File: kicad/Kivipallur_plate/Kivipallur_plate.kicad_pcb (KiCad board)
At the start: 2 copper layers, 158.1 x 105.3 mm, 12 parts

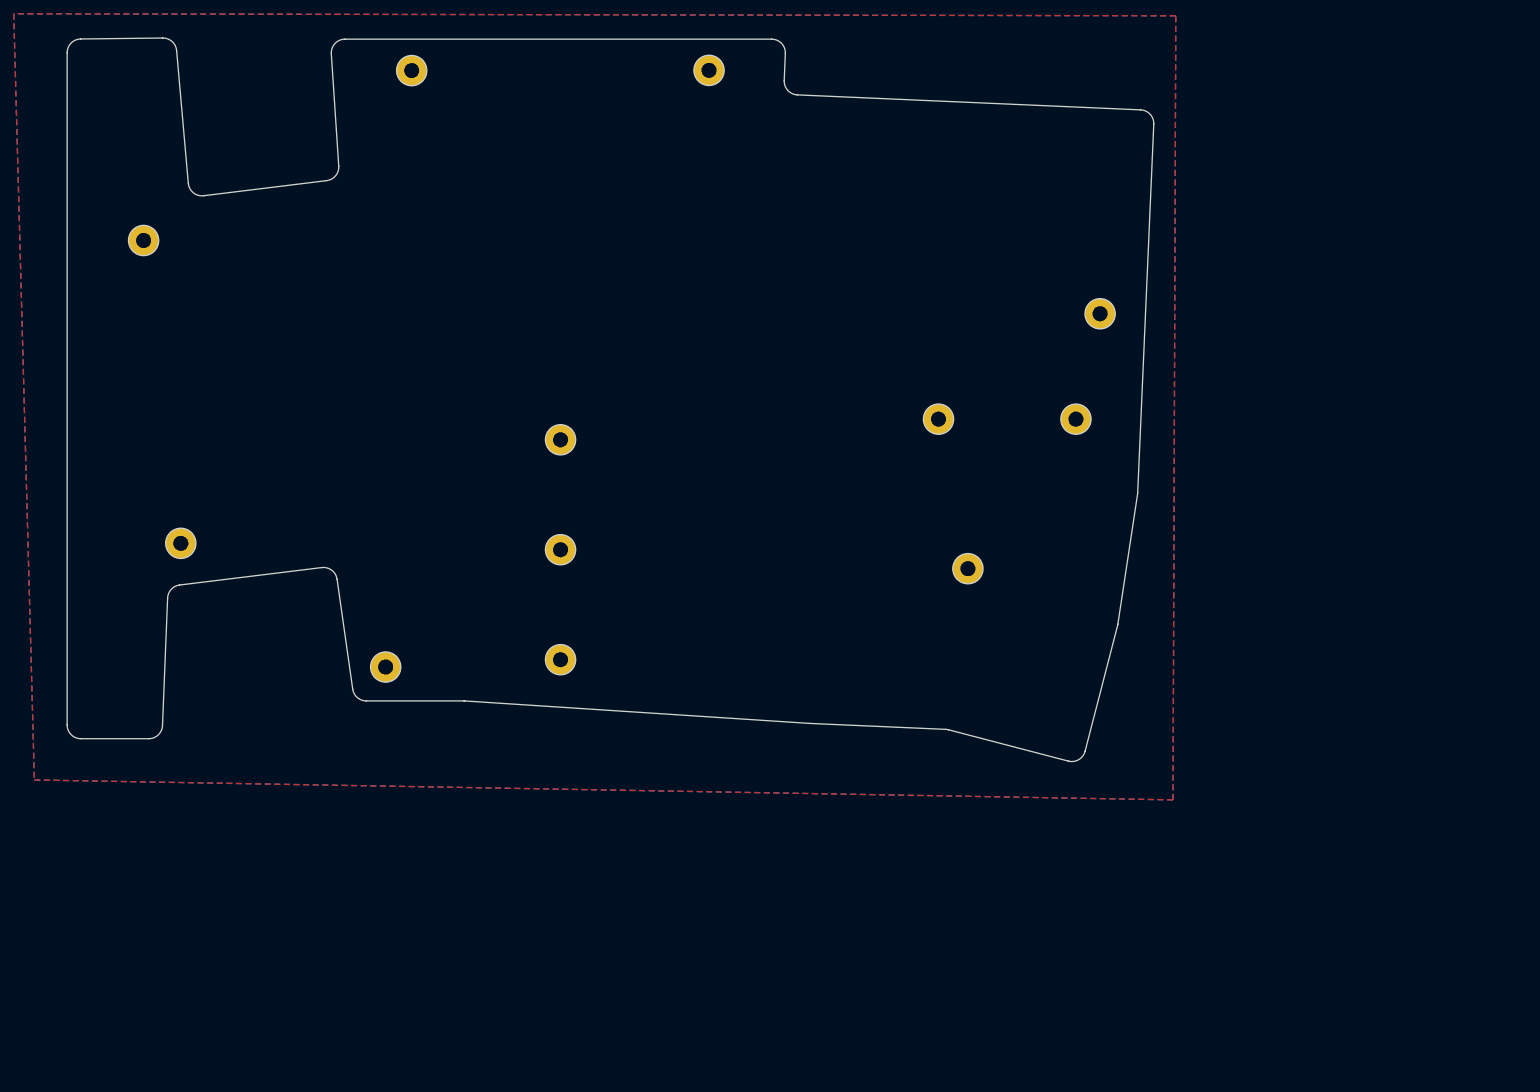
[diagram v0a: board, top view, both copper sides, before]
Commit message: Change PMW3360 footprint outline, finalize others
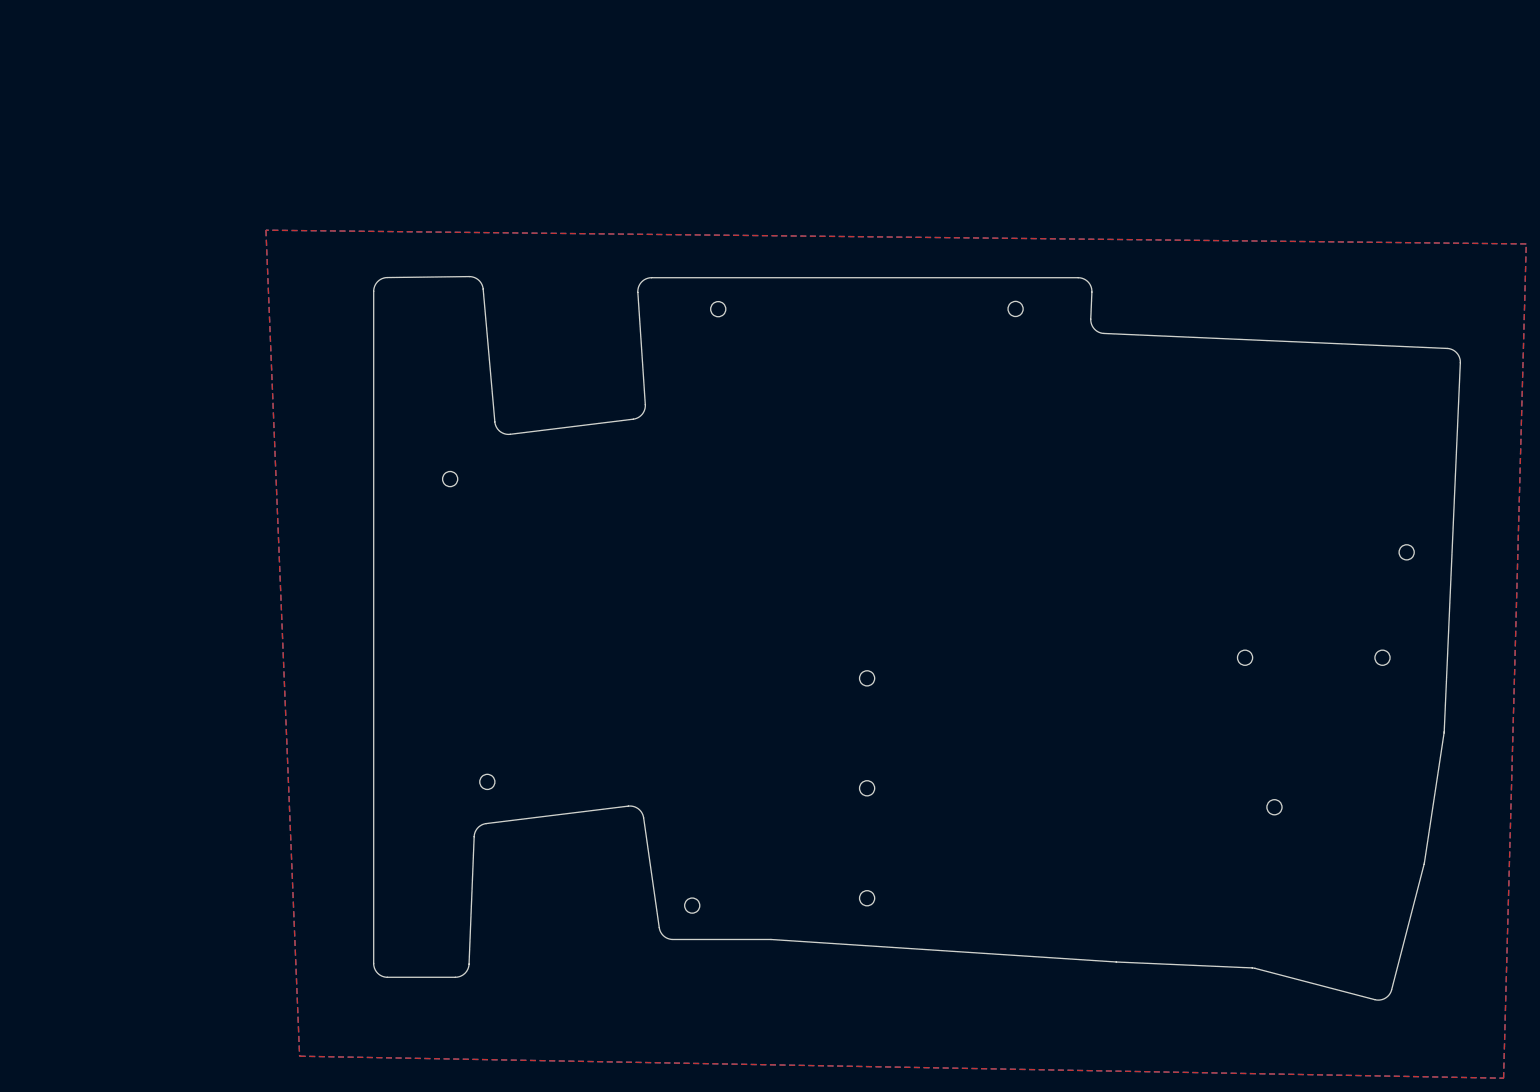
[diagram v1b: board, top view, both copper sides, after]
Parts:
- H1, H10, H11, H12, H2, H3, H4, H5, H6, H7, H8, H9: footprint MountingHole:MountingHole_2.2mm_M2_Pad -> MountingHole:MountingHole_2.2mm_M2
- moved H9 130.9 mm to (243.4, 154.6)
- moved H2 125.5 mm to (158.6, 168.9)
- moved H3 112.4 mm to (184.1, 167.8)
- moved H12 99.6 mm to (239.1, 132.8)
- moved H1 94.5 mm to (205.7, 82.1)
- moved H5 76.5 mm to (128.8, 150.9)
- moved H11 73.3 mm to (259.1, 132.8)
- moved H10 56.5 mm to (262.6, 117.5)
- moved H6 56.5 mm to (184.1, 151.8)
- moved H7 48.4 mm to (184.1, 135.8)
- moved H4 34.8 mm to (162.4, 82.1)
- moved H8 17.1 mm to (123.4, 106.8)
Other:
- outline, holes or cut-outs redrawn
